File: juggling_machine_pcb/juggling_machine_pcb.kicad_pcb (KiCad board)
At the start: 2 copper layers, 97 x 95 mm, 16 parts, among them J1 Conn_01x08, J10 Screw_Terminal_01x04, J11 Screw_Terminal_01x04, J2 Conn_01x08, J3 Conn_01x08, J4 Conn_01x08, J5 servo 1, J6 servo 2, J7 24v input, J8 5v input, J9 24v out for input to buck

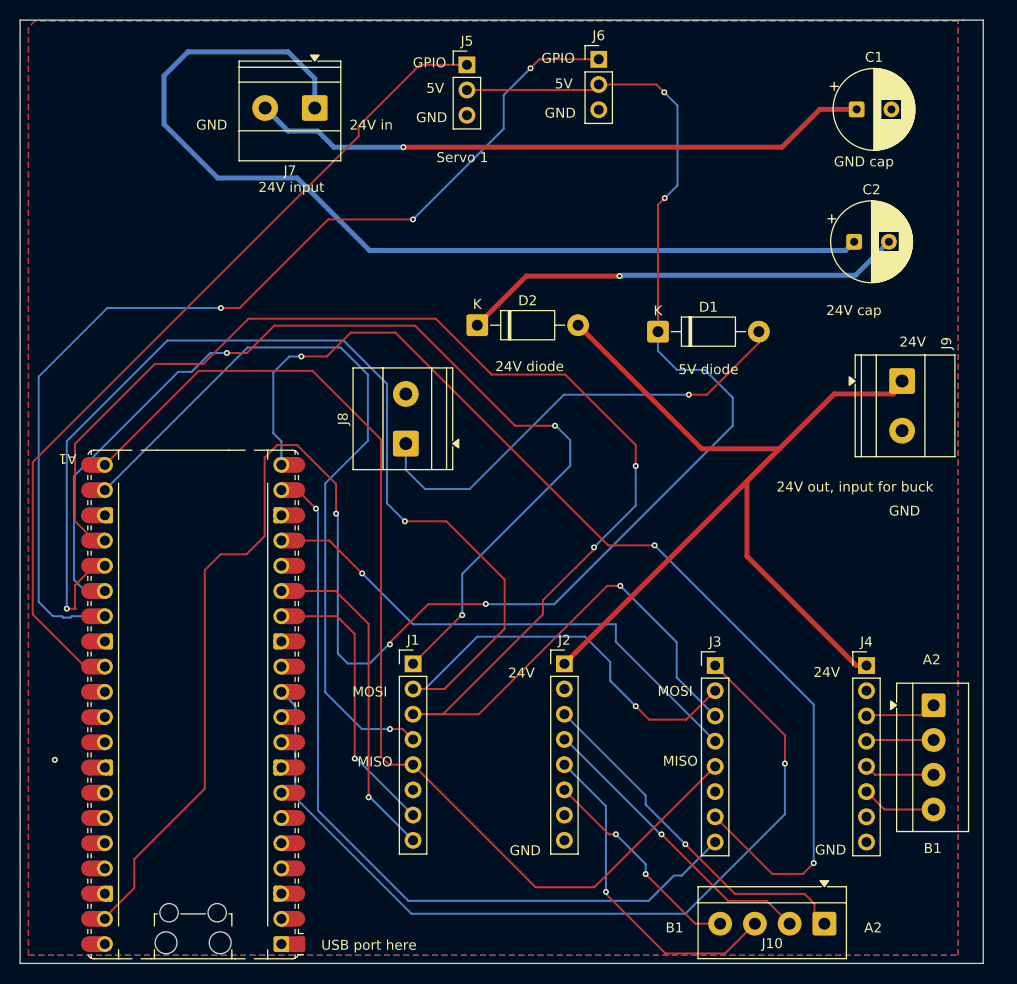
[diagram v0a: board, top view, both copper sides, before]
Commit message: rerouted pcb with new motor driver footprint
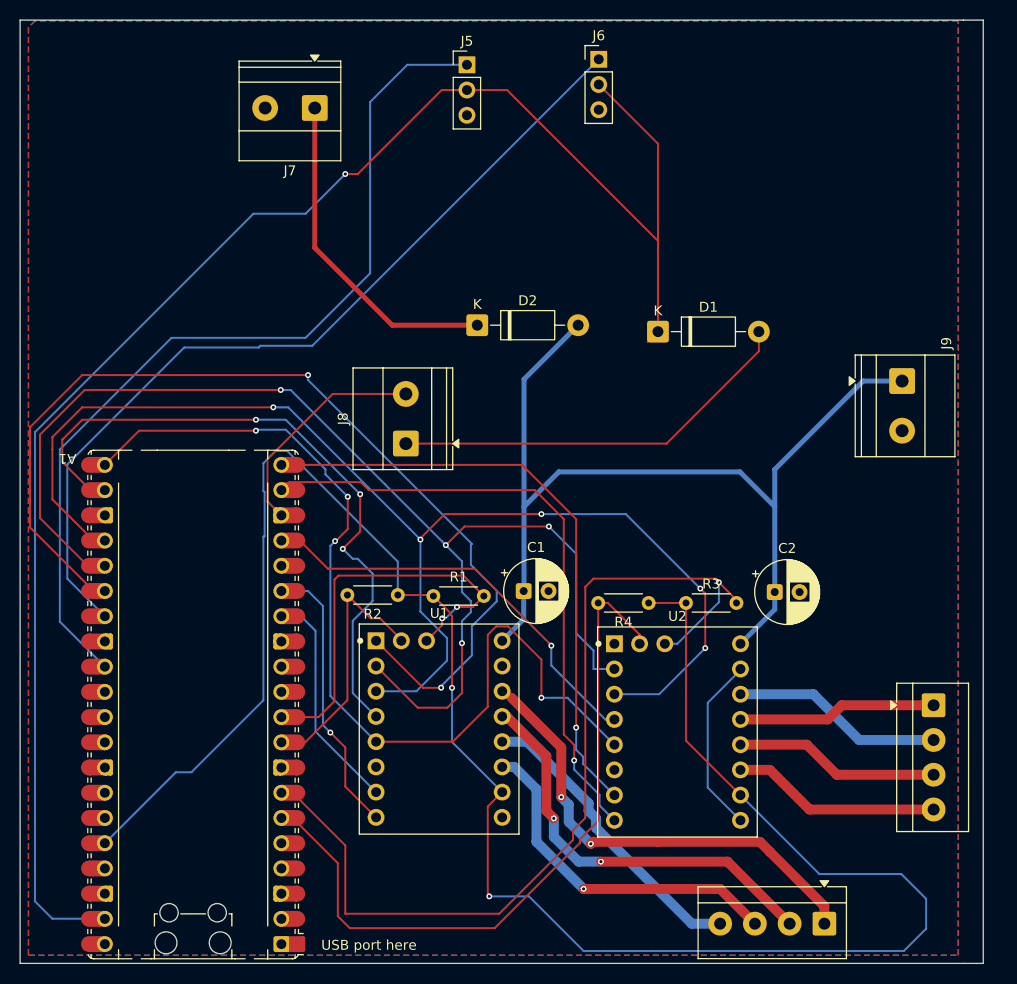
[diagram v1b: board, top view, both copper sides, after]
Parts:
- removed J1, J2, J3, J4: Conn_01x08, Connector_PinHeader_2.54mm:PinHeader_1x08_P2.54mm_Vertical
- added R1: 10k, Resistor_THT:R_Axial_DIN0204_L3.6mm_D1.6mm_P5.08mm_Horizontal, F.Cu at (91.6, 83.0)
- added R2: 10k, Resistor_THT:R_Axial_DIN0204_L3.6mm_D1.6mm_P5.08mm_Horizontal, F.Cu at (88.0, 82.9)
- added R3: 10k, Resistor_THT:R_Axial_DIN0204_L3.6mm_D1.6mm_P5.08mm_Horizontal, F.Cu at (117.1, 83.7)
- added R4: 10k, Resistor_THT:R_Axial_DIN0204_L3.6mm_D1.6mm_P5.08mm_Horizontal, F.Cu at (113.3, 83.7)
- added U1: TMC5160T_Pro_V1.1, tmc driver:BTT_TMC5160T_Pro_V1.1, F.Cu at (92.2, 96.4)
- added U2: TMC5160T_Pro_V1.1, tmc driver:BTT_TMC5160T_Pro_V1.1, F.Cu at (116.2, 96.7)
- C1, C2: value C_Polarized -> C; footprint Capacitor_THT:CP_Radial_D8.0mm_P3.50mm -> Capacitor_THT:CP_Radial_D6.3mm_P2.50mm
- moved C1 59.0 mm to (100.7, 82.5)
- moved C2 36.2 mm to (126.0, 82.6)
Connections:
- net Net-(A1-GPIO21) renamed Servo 2
- net Net-(A1-GPIO22) renamed Servo 1
- A1 pad 10: unconnected-(A1-GPIO7-Pad10) -> DIAG1.1
- A1 pad 11: Net-(A1-GPIO8) -> unconnected-(A1-GPIO8-Pad11)
- A1 pad 14: Net-(A1-GPIO10) -> STEP 1
- A1 pad 15: Net-(A1-GPIO11) -> DIR 1
- A1 pad 17: Net-(A1-GPIO13) -> CSN 2
- A1 pad 19: Net-(A1-GPIO14) -> DIR 2
- A1 pad 20: Net-(A1-GPIO15) -> STEP 2
- A1 pad 22: Net-(A1-GPIO17) -> CSN 1
- A1 pad 26: Net-(A1-GPIO20) -> EN 1
- A1 pad 6: unconnected-(A1-GPIO4-Pad6) -> DIAG0.2
- A1 pad 7: unconnected-(A1-GPIO5-Pad7) -> DIAG1.2
- A1 pad 9: unconnected-(A1-GPIO6-Pad9) -> DIAG0.1
- C1 pad 1: Net-(J7-Pin_2) -> +24V
- C2 pad 1: Net-(J7-Pin_1) -> +24V
- C2 pad 2: Net-(D2-K) -> GND
- J10 pad 1: Net-(J10-Pin_1) -> A2.1
- J10 pad 2: Net-(J10-Pin_2) -> A1.1
- J10 pad 3: Net-(J10-Pin_3) -> B2.1
- J10 pad 4: Net-(J10-Pin_4) -> B1.1
- J11 pad 1: Net-(J11-Pin_1) -> A2.2
- J11 pad 2: Net-(J11-Pin_2) -> A1.2
- J11 pad 3: Net-(J11-Pin_3) -> B2.2
- J11 pad 4: Net-(J11-Pin_4) -> B1.2
- J7 pad 1: Net-(J7-Pin_1) -> Net-(D2-K)
- J7 pad 2: Net-(J7-Pin_2) -> GND
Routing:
- net +3V3: track 0.00 -> 204.0 mm, vias 0 -> 2
- net Net-(A1-GPIO15): track 110.0 -> 0.00 mm, vias 3 -> 0
- net Net-(A1-GPIO20): track 104.2 -> 0.00 mm, vias 3 -> 0
- net EN 1: track 0.00 -> 100.7 mm, vias 0 -> 2
- net Net-(J7-Pin_1): track 100.3 -> 0.00 mm
- net DIAG1.2: track 0.00 -> 93.8 mm, vias 0 -> 1
- net Net-(A1-GPIO8): track 87.4 -> 0.00 mm, vias 1 -> 0
- net Net-(A1-GPIO14): track 80.2 -> 0.00 mm, vias 1 -> 0
- net Net-(A1-GPIO17): track 78.2 -> 0.00 mm, vias 1 -> 0
- net DIAG0.2: track 0.00 -> 72.9 mm
- net CSN 1: track 0.00 -> 68.1 mm, vias 0 -> 3
- net Net-(J7-Pin_2): track 62.9 -> 0.00 mm, vias 1 -> 0
- net DIR 2: track 0.00 -> 62.8 mm, vias 0 -> 1
- net STEP 2: track 0.00 -> 61.3 mm, vias 0 -> 1
- net Net-(A1-GPIO13): track 52.3 -> 0.00 mm, vias 1 -> 0
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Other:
- board text removed: "24V"
- board text removed: "24V cap"
- board text removed: "24V diode"
- board text removed: "24V in"
- board text removed: "24V input"
- board text removed: "24V out, input for buck"
- board text removed: "5V"
- board text removed: "5V diode"
- board text removed: "A2"
- board text removed: "B1"
- board text removed: "GND"
- board text removed: "GND cap"
- board text removed: "GPIO"
- board text removed: "MISO"
- board text removed: "MOSI"
- board text removed: "Servo 1"
- board text removed: "Stepper driver 1"
- board text removed: "Stepper driver 2"
